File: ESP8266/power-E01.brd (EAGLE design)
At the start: 26 x 19.1 mm, 12 parts, among them CON1 USBMICRO-NO_CENTER

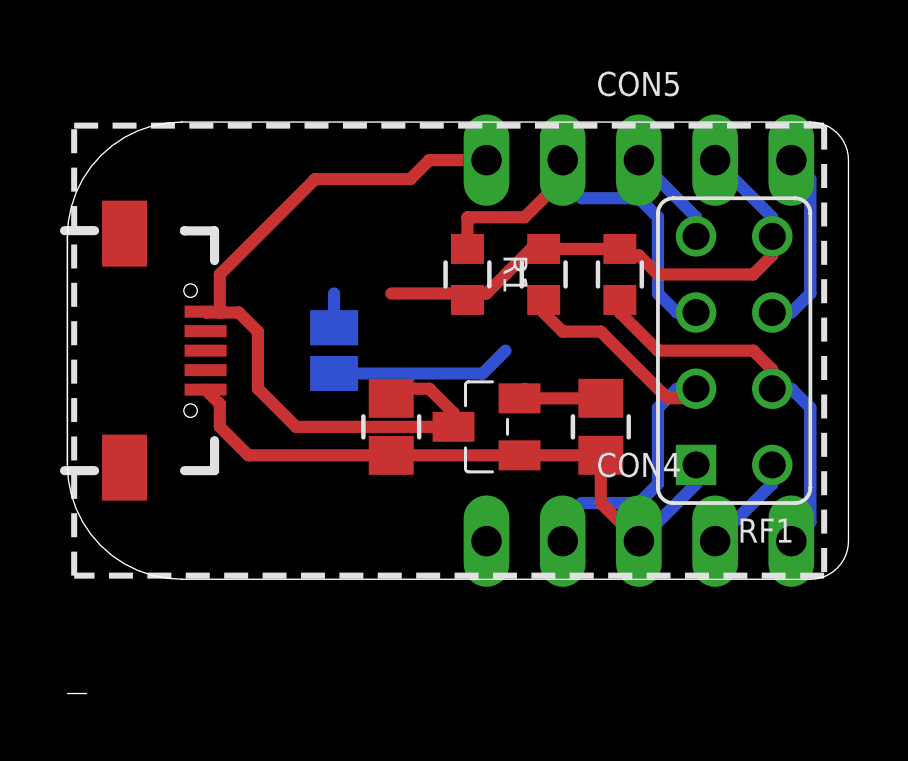
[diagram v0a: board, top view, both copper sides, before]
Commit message: Added some adapters for ESP8266 01 module
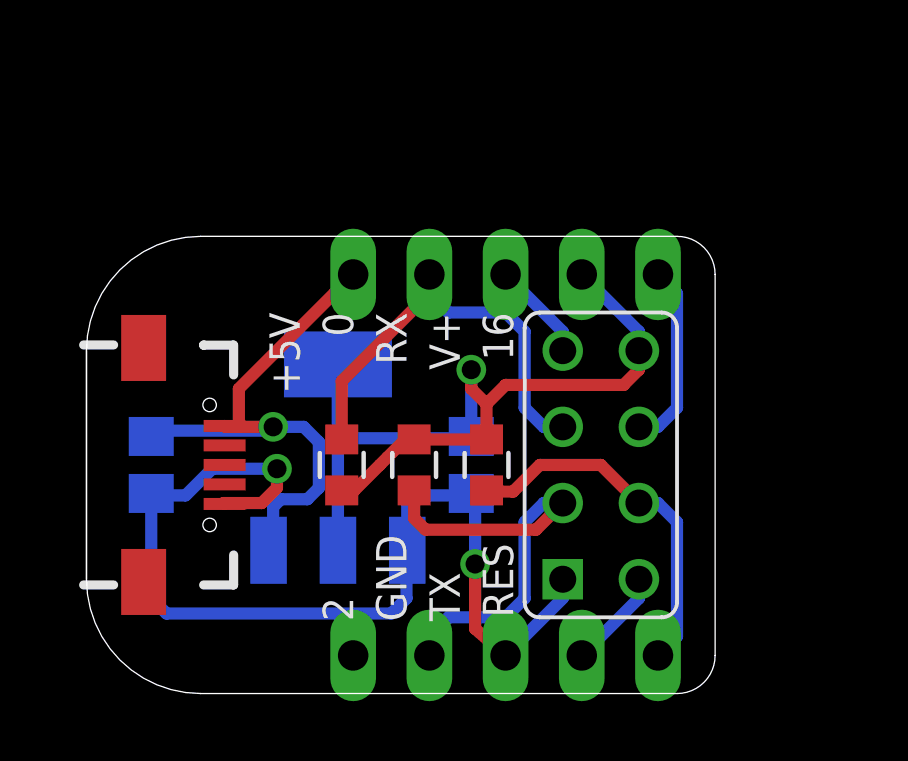
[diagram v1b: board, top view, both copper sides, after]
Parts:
- removed C1, C2: 1uF, p.peter-rcl:C0805
- removed SJ1: (no value), jumper:SJ
- removed U1: (no value), p.peter-regulators:SOT23
- added C7: 10u, p.peter-rcl:C0805
- added C8: 22u, p.peter-rcl:C0805
- added IC1: (no value), p.peter-regulators:SOT223
- RF1: device p.peter-periphery:ESP8266-ESP-01 -> p.peter-periphery:ESP8266-ESP-01-NOSILK
- moved R3 7.75 mm to (13.3, 7.62)
- moved R2 7.68 mm to (10.9, 7.62)
- moved R1 7.61 mm to (8.51, 7.62)
- moved RF1 5.85 mm to (17.1, 7.62)
- moved CON5 5.85 mm to (14.0, 14.0)
- moved CON4 5.85 mm to (14.0, 1.27)
- moved CON1 3.86 mm to (3.17, 7.62)
- moved U$3 3.70 mm to (3.43, 12.4), turned to 0 degrees
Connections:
- removed net N$1: C2.1, SJ1.1, U1.P$2
- net +3V3: now also C8.2, IC1.2, IC1.4; no longer SJ1.2
- net +5V: now also C7.2, IC1.3; no longer C1.1, U1.P$3
- net GND: now also C7.1, C8.1, IC1.1; no longer C1.2, C2.2, U1.P$1
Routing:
- net +3V3: track 19.5 -> 34.1 mm, vias 0 -> 1
- net GND: track 21.2 -> 34.9 mm, vias 0 -> 2
- net N$1: track 9.13 -> 0.00 mm
- net +5V: track 25.7 -> 19.6 mm, vias 0 -> 1
- net IO00: track 13.8 -> 15.1 mm
- net RESET: track 13.2 -> 12.2 mm
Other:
- board size 26 x 19.1 mm -> 21 x 15.2 mm
- board text added: "0"
- board text added: "16"
- board text added: "2"
- board text removed: "DAT"
- board text removed: "ESP-WS2812 ADAPTER"
- board text removed: "FL"
- board text removed: "justgeek.de"
